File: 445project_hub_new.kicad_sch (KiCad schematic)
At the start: 46 parts, among them J101 Barrel_Jack_Switch, J102 USB_B, J104 USB, SW101 SW_Push, U101 MCP1826S, U102 SN75240, U103 TUSB2046I, U105 SN75240, Y101 6MHz

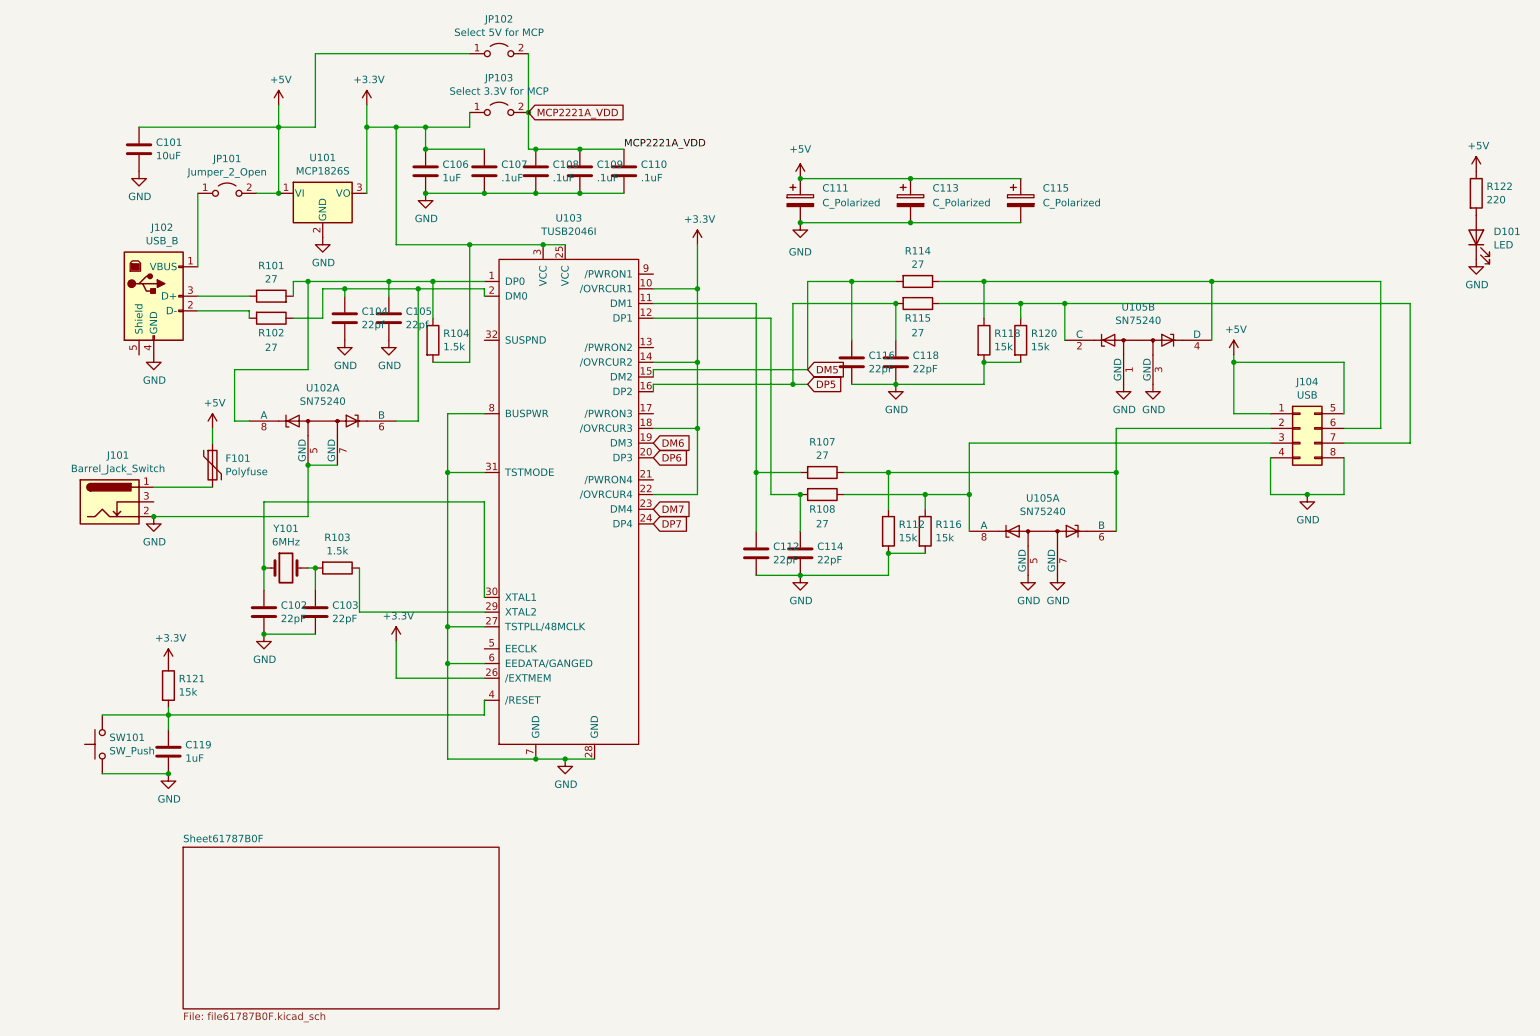
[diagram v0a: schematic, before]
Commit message: New Central Hub: Add USB-C, 5V->3.3V regulator
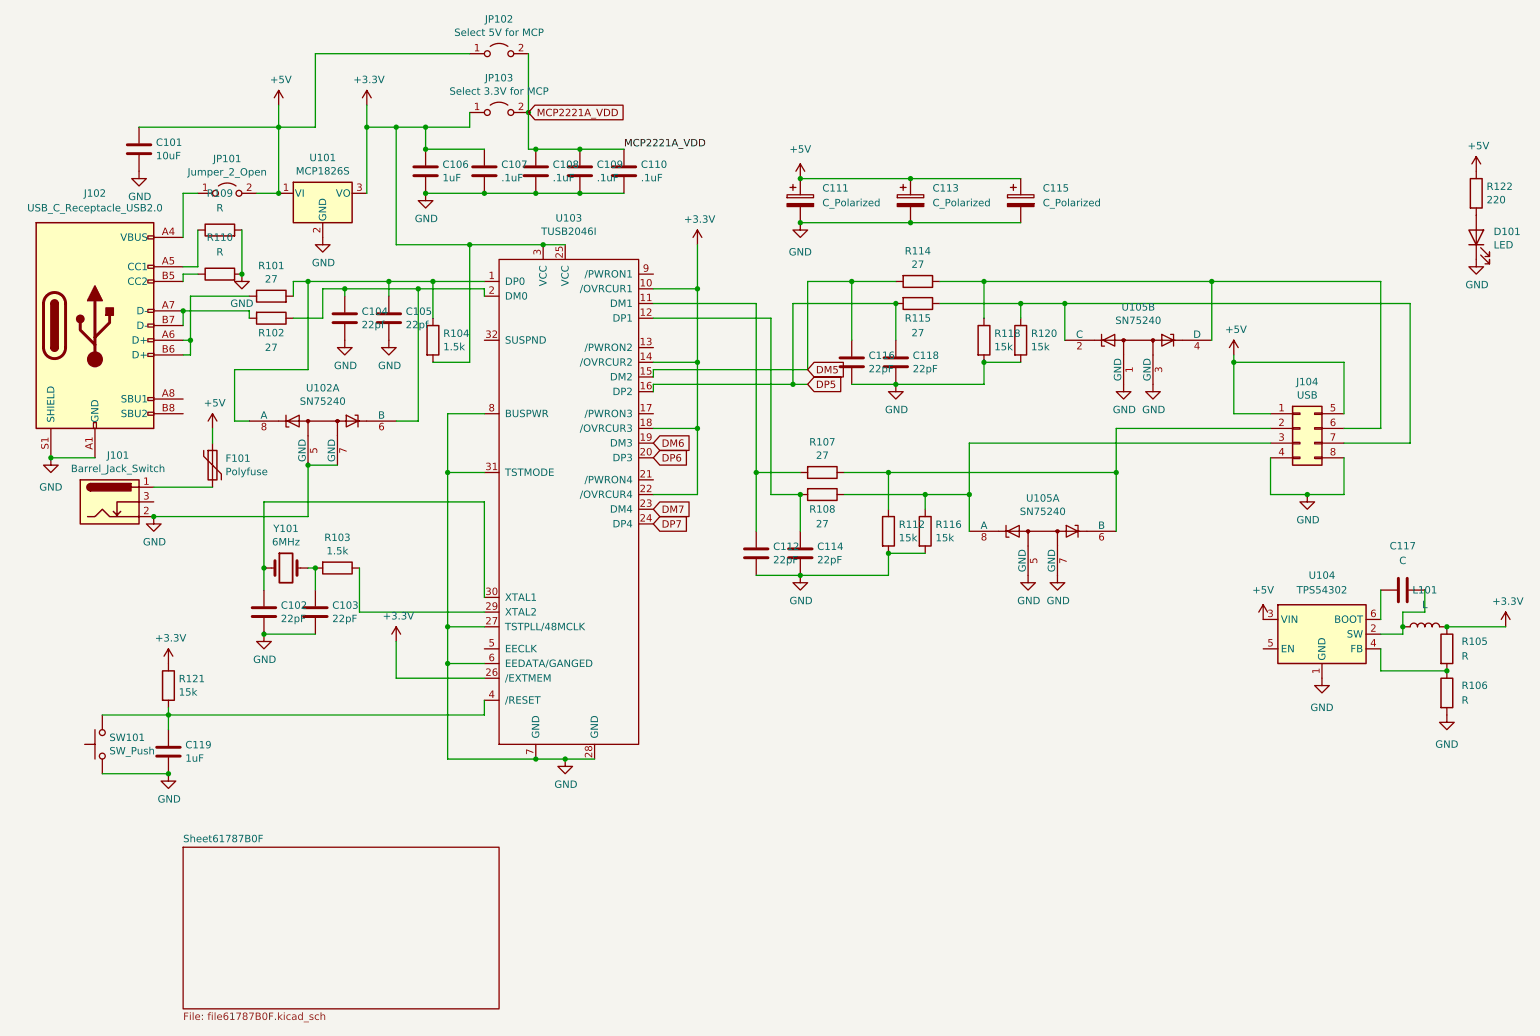
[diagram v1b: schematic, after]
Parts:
- removed J102: USB_B, Connector_USB:USB_B_OST_USB-B1HSxx_Horizontal, symbol 445project_hub_new-rescue:USB_B-Connector-445project_hub-rescue
- added C117: C, Capacitor_SMD:C_0603_1608Metric, symbol Device:C
- added J102: USB_C_Receptacle_USB2.0, Library:USB_C_Receptacle_GCT_USB4105-xx-A_16P_TopMnt_Horizontal, symbol Connector:USB_C_Receptacle_USB2.0
- added L101: L, Inductor_SMD:L_7.3x7.3_H3.5, symbol Device:L
- added R105, R106, R109, R110: R, Resistor_SMD:R_0603_1608Metric, symbol Device:R
- added U104: TPS54302, Package_TO_SOT_SMD:SOT-23-6, symbol Regulator_Switching:TPS54302
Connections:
- net +3V3: now also L101.2, R105.1
- net +5V: now also U104.3 (VIN)
- net GND: now also J102.A1 (GND), J102.A12 (GND), J102.B1 (GND), J102.B12 (GND), J102.S1 (SHIELD), R106.2, R109.2, R110.2, U104.1 (GND)
- net at JP101.1 (A): now also J102.A4 (VBUS), J102.A9 (VBUS), J102.B4 (VBUS), J102.B9 (VBUS)
- net at R102.2: now also J102.A7 (D-), J102.B7 (D-)
- net at R101.1: now also J102.A6 (D+), J102.B6 (D+)
- new net: R105.2, R106.1, U104.4 (FB)
- new net: J102.A5 (CC1), R109.1
- new net: J102.B5 (CC2), R110.1
- new net: C117.1, U104.6 (BOOT)
- new net: C117.2, L101.1, U104.2 (SW)
